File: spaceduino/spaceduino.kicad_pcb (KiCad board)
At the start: 2 copper layers, 69 x 69 mm, 76 parts, among them J1 USB_B, J3 JICSP, J4 Conn_02x05_Odd_Even, Q1 BSS84, Q2 BSS84, Q3 BSS84, SW1 SW_SPST, U1 TLV70030_SOT23-5, U2 FT230XS, U3 TXB0104D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

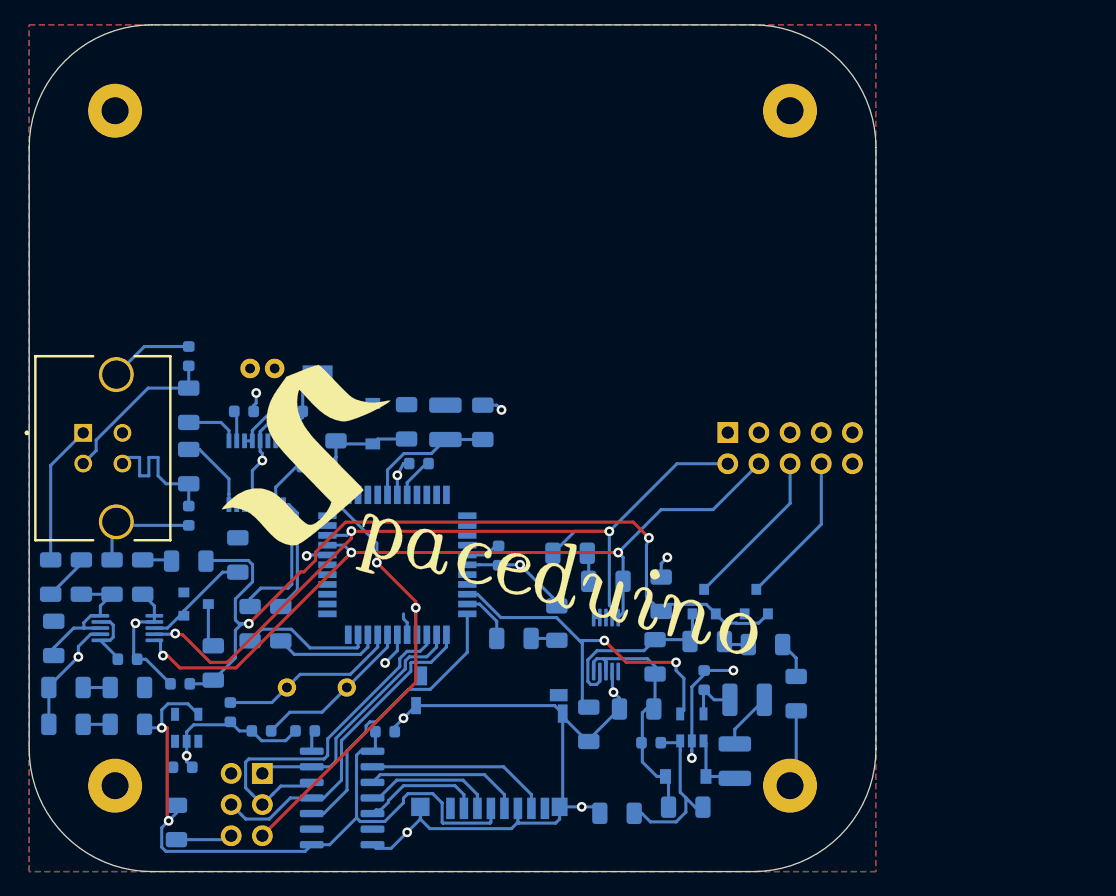
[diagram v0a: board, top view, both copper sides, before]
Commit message: add SD card footprint, PNP-based current mirror
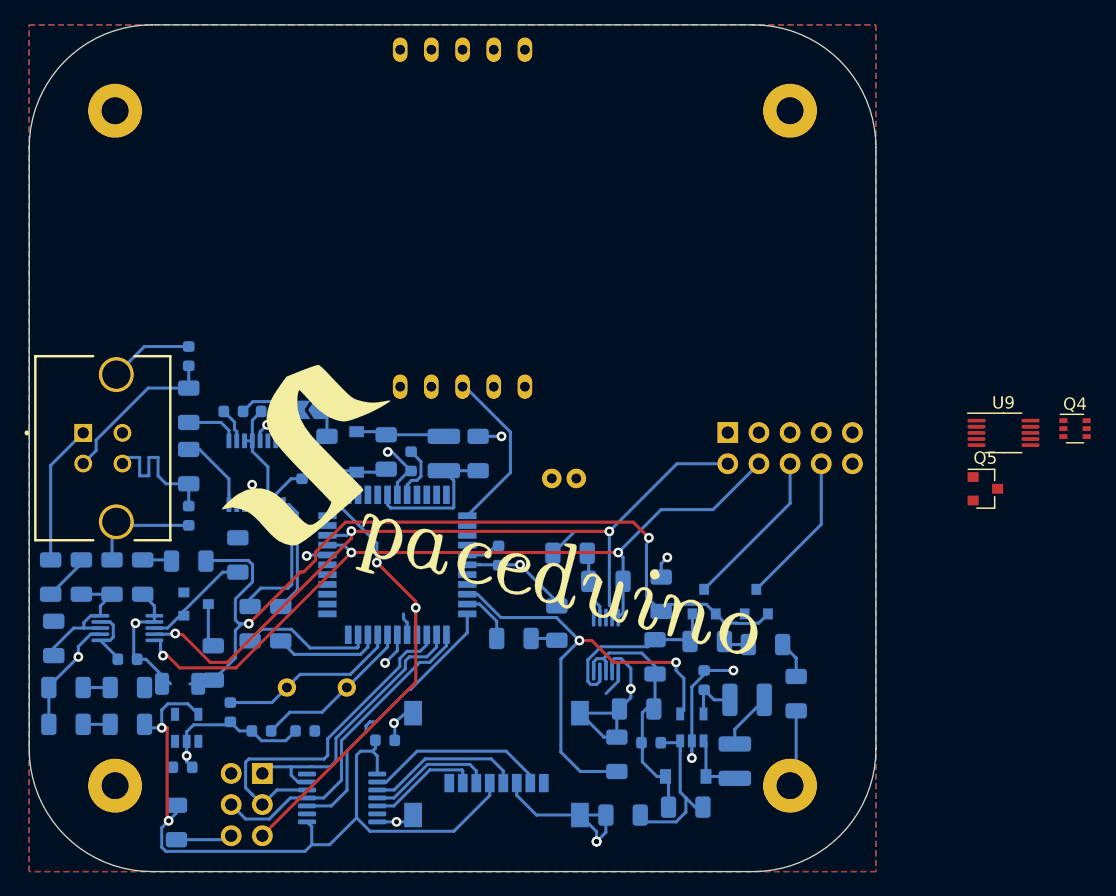
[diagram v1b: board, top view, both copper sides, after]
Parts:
- added Q4: BC856BS, Package_TO_SOT_SMD:SOT-363_SC-70-6, F.Cu at (141.2, 88.9)
- added Q5: BSS84, Package_TO_SOT_SMD:SOT-23, F.Cu at (133.9, 93.8)
- added U8: MPD200A, Spaceduino:MPD200A, B.Cu at (91.3, 71.8)
- added U9: INA226, Package_SO:VSSOP-10_3x3mm_P0.5mm, F.Cu at (135.4, 89.2)
- C18: footprint Capacitor_SMD:C_0603_1608Metric -> Capacitor_SMD:C_1206_3216Metric
- L1: value L -> 10uH
- MICROSD1: footprint Connector_Card:microSD_HC_Hirose_DM3D-SF -> Spaceduino:Connfly DS1139-06 MicroSD
- U3: footprint Package_SO:SOIC-14_3.9x8.7mm_P1.27mm -> Package_SO:TSSOP-14_4.4x5mm_P0.65mm
- moved C21 26.2 mm to (100.6, 93.0)
- moved R21 3.35 mm to (103.9, 115.4), turned to 90 degrees
- moved R5 2.96 mm to (85.1, 90.8)
- moved SW1 2.92 mm to (79.0, 87.4)
- moved MICROSD1 2.66 mm to (90.9, 115.2)
- moved D1 2.66 mm to (82.7, 90.8)
- moved C8 2.57 mm to (92.6, 90.9)
- moved L1 2.54 mm to (89.8, 90.9)
- moved R19 2.54 mm to (80.3, 90.9)
- moved C1 1.81 mm to (75.7, 87.5)
- moved C2 0.86 mm to (72.6, 87.5)
- moved C5 0.79 mm to (78.2, 92.2), turned to 270 degrees
- moved C20 0.70 mm to (85.0, 114.3)
- moved C16 0.65 mm to (87.1, 91.6), turned to 270 degrees
- moved R9 0.52 mm to (104.4, 120.4)
- renumbered D3 to DBPWR2
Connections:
- J4 pad 1: Net-(J4-Pad1) -> GND
- J4 pad 3: Net-(J4-Pad3) -> experiment
- J4 pad 5: Net-(J4-Pad5) -> HV-
- J4 pad 7: Net-(J4-Pad7) -> HV+
- J4 pad 9: Net-(J4-Pad9) -> GND
- MICROSD1 pad 9: Net-(MICROSD1-Pad9) -> GND
- U6 pad 34: a3 -> a3_pump_en
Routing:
- net GND: track 163.9 -> 140.9 mm, vias 17 -> 18
- net +5V: track 23.5 -> 38.0 mm
- net a3_pump_en: track 0.00 -> 13.7 mm
- net 2_boost_en: track 29.6 -> 38.8 mm
- net ~reset: track 49.8 -> 47.6 mm
- net 6_spi_miso: track 20.9 -> 23.1 mm
- net Net-(C8-Pad1): track 10.8 -> 12.5 mm
- net +3V0: track 59.2 -> 60.7 mm
- net Net-(C16-Pad1): track 3.38 -> 4.57 mm
- net 4_sd_ss: track 23.4 -> 22.6 mm
- net Net-(C5-Pad2): track 4.24 -> 3.52 mm
- net Net-(MICROSD1-Pad2): track 9.89 -> 9.22 mm
- net 7_spi_sck: track 29.5 -> 28.9 mm
- net Net-(C15-Pad2): track 14.1 -> 13.5 mm
- net Net-(R19-Pad1): track 2.92 -> 2.38 mm

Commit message: Filled some traces for Q4 and U6, need thicker power trace
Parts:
- moved U9 25.7 mm to (110.0, 85.4)
- moved Q4 25.7 mm to (115.8, 85.1)
- moved Q5 17.1 mm to (119.4, 102.9)
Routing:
- net +5V: track 38.0 -> 63.9 mm, vias 0 -> 1
- net i2c_sda: track 69.3 -> 79.2 mm
- net i2c_scl: track 65.5 -> 75.4 mm
- net experiment: track 0.00 -> 6.53 mm
- net Net-(Q4-Pad2): track 0.00 -> 2.55 mm
- net GND: track 140.9 -> 141.4 mm
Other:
- net class Power added: clearance 0.2, trace_width 1, via_dia 0.8, via_drill 0.4
- rule trace_min: 0.2 -> 0.25

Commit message: spaceduino laid out???
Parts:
- removed MICROSD1: Micro_SD_Card_Det, Spaceduino:Connfly DS1139-06 MicroSD
- added J2: Micro_SD_Card, Spaceduino:MOLEX_500901-0801, B.Cu at (94.6, 120.1)
- added R22: 50m, Resistor_SMD:R_1206_3216Metric, B.Cu at (109.1, 82.4)
- added R23: 10, Resistor_SMD:R_1206_3216Metric, B.Cu at (107.3, 89.6)
- added R24: 10, Resistor_SMD:R_1206_3216Metric, B.Cu at (113.9, 82.4)
- added R25: 27, Resistor_SMD:R_1206_3216Metric, B.Cu at (118.9, 82.2)
- added R26: 10k, Resistor_SMD:R_1206_3216Metric, B.Cu at (120.1, 85.4)
- added R27: 10k, Resistor_SMD:R_1206_3216Metric, B.Cu at (103.6, 88.5)
- added RV1: R_POT, Potentiometer_THT:Potentiometer_Bourns_3296Y_Vertical, F.Cu at (116.0, 76.8)
- Q4, Q5, U9: moved to B.Cu
- moved Q5 18.9 mm to (104.1, 91.6), turned to 270 degrees
- moved R9 5.40 mm to (109.5, 122.2)
- moved C21 1.11 mm to (99.5, 93.2)
- moved C18 1.11 mm to (68.6, 108.6), turned to 270 degrees
- moved R21 0.09 mm to (103.8, 115.4), turned to 270 degrees
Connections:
- J4 pad 7: HV+ -> GND
- J4 pad 9: GND -> HV+
- Q5 pad 1: Net-(Q5-Pad1) -> a2_exp_en
- U6 pad 35: a2 -> a2_exp_en
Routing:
- net HV-: track 0.00 -> 70.4 mm
- net HV+: track 0.00 -> 55.7 mm
- net GND: track 141.4 -> 166.9 mm, vias 18 -> 21
- net a2_exp_en: track 0.00 -> 17.1 mm
- net Net-(Q4-Pad2): track 2.55 -> 15.1 mm
- net Net-(Q4-Pad1): track 0.00 -> 8.61 mm
- net +5V: track 63.9 -> 55.5 mm, vias 1 -> 3
- net Net-(R22-Pad2): track 0.00 -> 6.77 mm
- net Net-(R25-Pad1): track 0.00 -> 5.98 mm
- net 2_boost_en: track 38.8 -> 34.1 mm
- net i2c_scl: track 75.4 -> 78.6 mm, vias 3 -> 4
- net +3V0: track 60.7 -> 63.8 mm
- net Net-(C15-Pad2): track 13.5 -> 10.6 mm
- net Net-(Q4-Pad4): track 0.00 -> 2.62 mm
- net Net-(Q5-Pad2): track 0.00 -> 2.34 mm
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
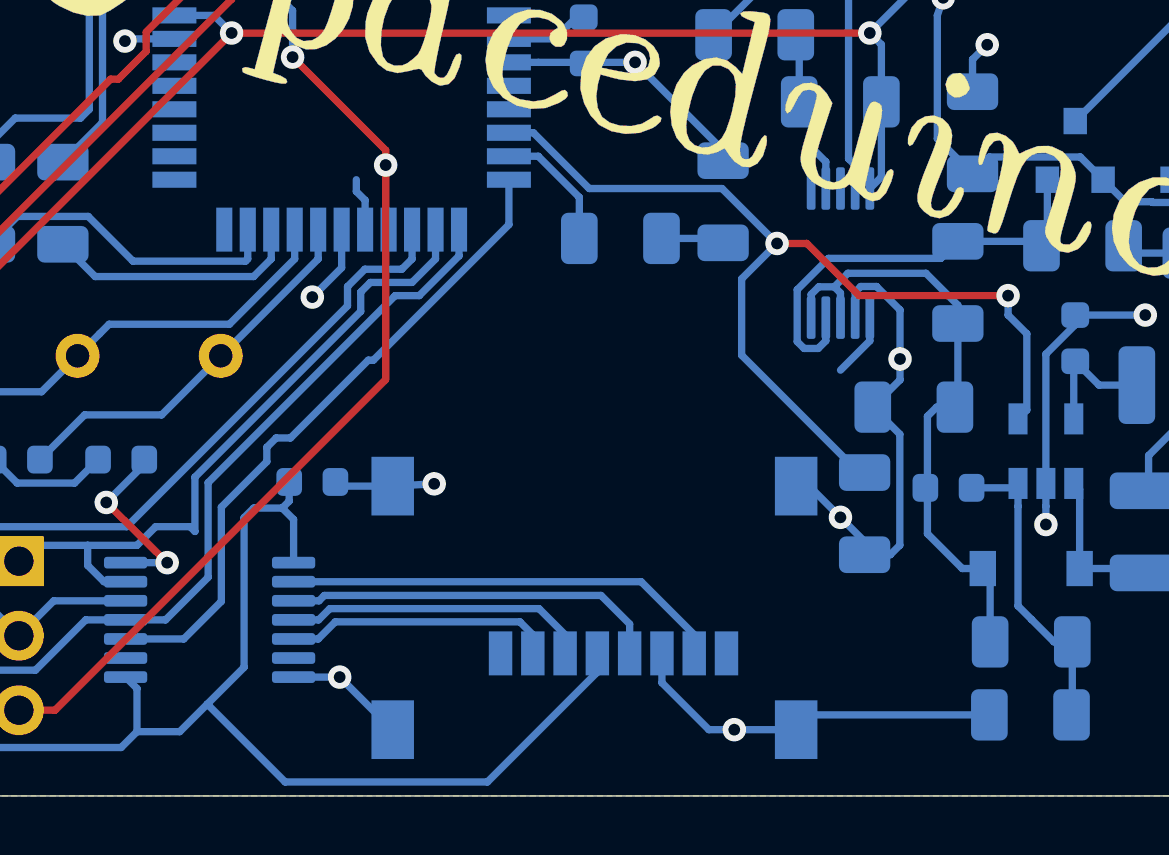
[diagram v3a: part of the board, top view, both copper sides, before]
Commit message: use sd card that is actually in stock on digikey
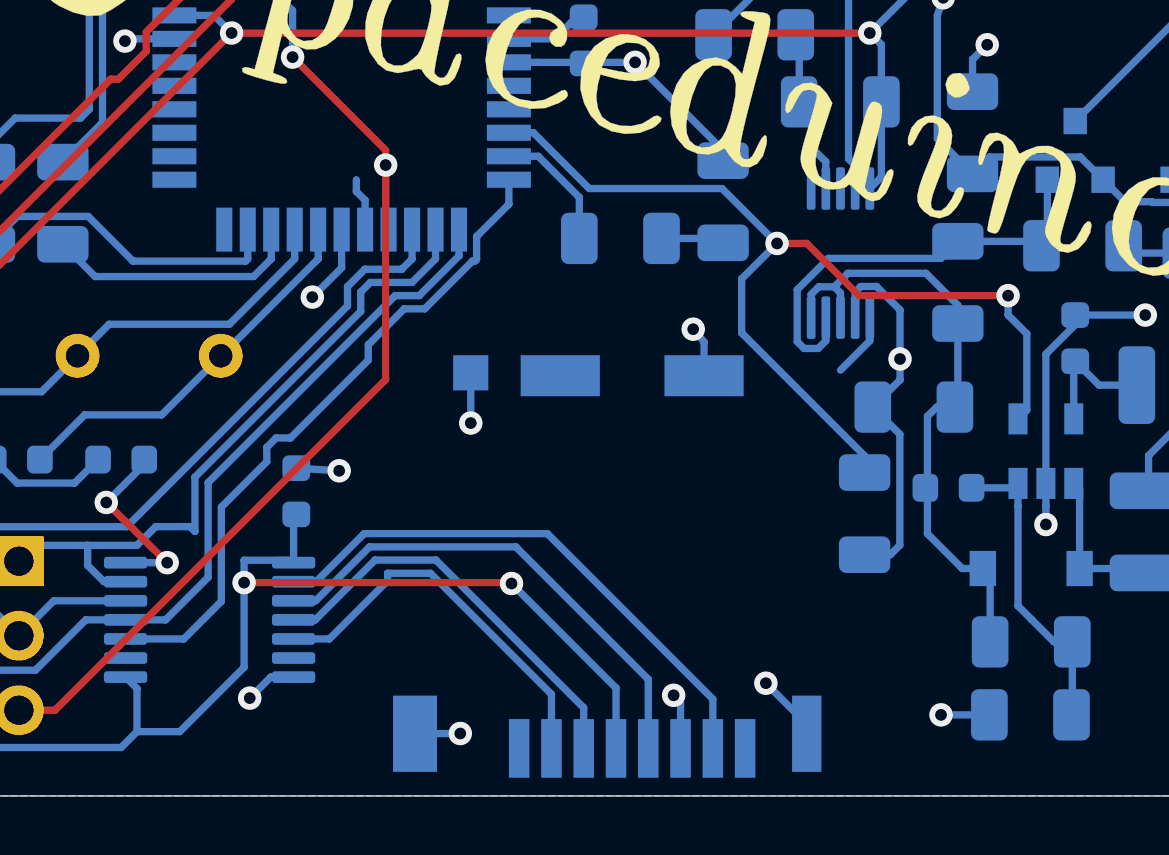
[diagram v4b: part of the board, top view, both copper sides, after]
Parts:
- J2: footprint Spaceduino:MOLEX_500901-0801 -> Spaceduino:HRS_DM3CS-SF
- moved J2 3.18 mm to (95.2, 117.0), turned to 180 degrees
- moved C20 0.63 mm to (84.5, 114.6), turned to 90 degrees
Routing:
- net GND: track 166.9 -> 157.0 mm, vias 21 -> 25
- net Net-(J2-Pad2): track 9.21 -> 13.4 mm
- net Net-(J2-Pad5): track 12.9 -> 17.1 mm
- net Net-(J2-Pad7): track 15.0 -> 19.0 mm
- net Net-(J2-Pad3): track 10.9 -> 14.7 mm
- net +3V0: track 63.8 -> 61.1 mm, vias 2 -> 4

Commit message: can i get a go dawgs
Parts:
- moved R26 22.1 mm to (98.2, 88.6)
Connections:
- R22 pad 1: +5V -> Net-(Q5-Pad2)
- R23 pad 1: Net-(Q5-Pad2) -> +5V
- R26 pad 2: Net-(Q4-Pad2) -> a3_pump_en
- U9 pad 10: +5V -> Net-(Q5-Pad2)
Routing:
- net Net-(Q5-Pad2): track 2.34 -> 15.9 mm
- net a3_pump_en: track 13.7 -> 15.5 mm
- net +5V: track 55.5 -> 57.0 mm

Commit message: ordered it supposedly
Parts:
- C12: value .1uF -> 10uF; footprint Capacitor_SMD:C_0603_1608Metric -> Capacitor_SMD:C_1206_3216Metric
- D3PWR1, DALERT1, DBPWR1, DBPWR2, DIND1, DPWR1: footprint LED_SMD:LED_1206_3216Metric -> LED_SMD:LED_0603_1608Metric
- R10, R12, R14, R15, R16, R17, R18, R25, R3, R4, R7, R9: footprint Resistor_SMD:R_1206_3216Metric -> Resistor_SMD:R_0603_1608Metric
- RV1: moved to B.Cu
- moved RV1 2.95 mm to (117.3, 79.5)
- moved C1 1.77 mm to (75.2, 85.8), turned to 90 degrees
- moved C2 1.75 mm to (73.0, 85.8), turned to 270 degrees
- moved R8 0.80 mm to (72.6, 99.9)
- moved R14 0.65 mm to (111.1, 105.6)
- moved C12 0.43 mm to (111.0, 109.0)
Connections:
- Q5 pad 2: Net-(Q5-Pad2) -> +5V
- Q5 pad 3: +5V -> Net-(Q5-Pad3)
- R22 pad 1: Net-(Q5-Pad2) -> Net-(Q5-Pad3)
- U9 pad 10: Net-(Q5-Pad2) -> Net-(Q5-Pad3)
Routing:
- net +5V: track 57.0 -> 76.8 mm
- net Net-(Q5-Pad3): track 0.00 -> 19.1 mm
- net Net-(Q5-Pad2): track 15.9 -> 0.00 mm
- net GND: track 157.0 -> 150.9 mm, vias 25 -> 27
- net Net-(R25-Pad1): track 5.98 -> 3.42 mm
- net Net-(DBPWR1-Pad2): track 2.05 -> 3.79 mm
- net Net-(DBPWR1-Pad1): track 3.06 -> 4.28 mm
- net Net-(DPWR1-Pad2): track 2.20 -> 3.39 mm
- net Net-(DIND1-Pad2): track 2.16 -> 3.26 mm
- net Net-(DALERT1-Pad2): track 2.50 -> 3.58 mm
- net Net-(Q3-Pad1): track 8.91 -> 8.21 mm
- net Net-(D3PWR1-Pad2): track 2.20 -> 2.81 mm
- net Net-(C15-Pad2): track 10.6 -> 11.2 mm
- net d-: track 13.5 -> 14.0 mm
- net d+: track 12.0 -> 12.6 mm
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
